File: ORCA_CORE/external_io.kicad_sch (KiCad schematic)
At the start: 24 parts, among them J1 Vext_in, J2 6Vout, J3 6Vout, J4 6Vout, J5 6Vin, J6 Vext_out, J7 6Vout, P1 USB_C_Receptacle_USB2.0, SW1 SW_DPST_x2, U1 FT230XS

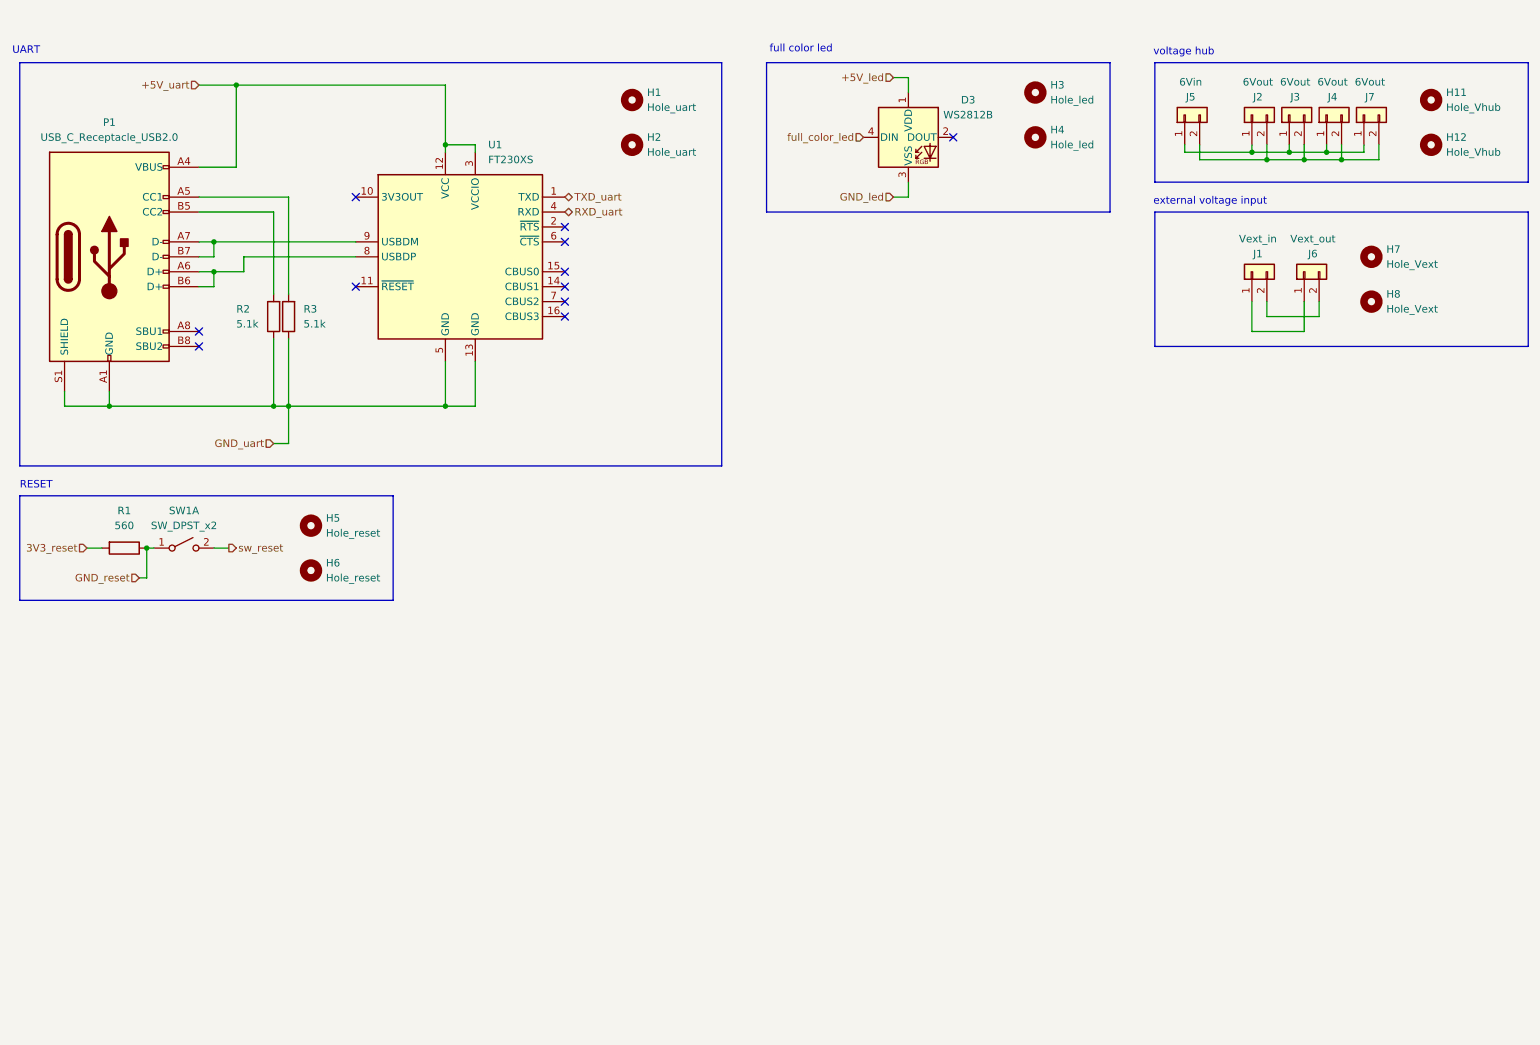
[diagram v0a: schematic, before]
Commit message: complete attaching footprint of CORE
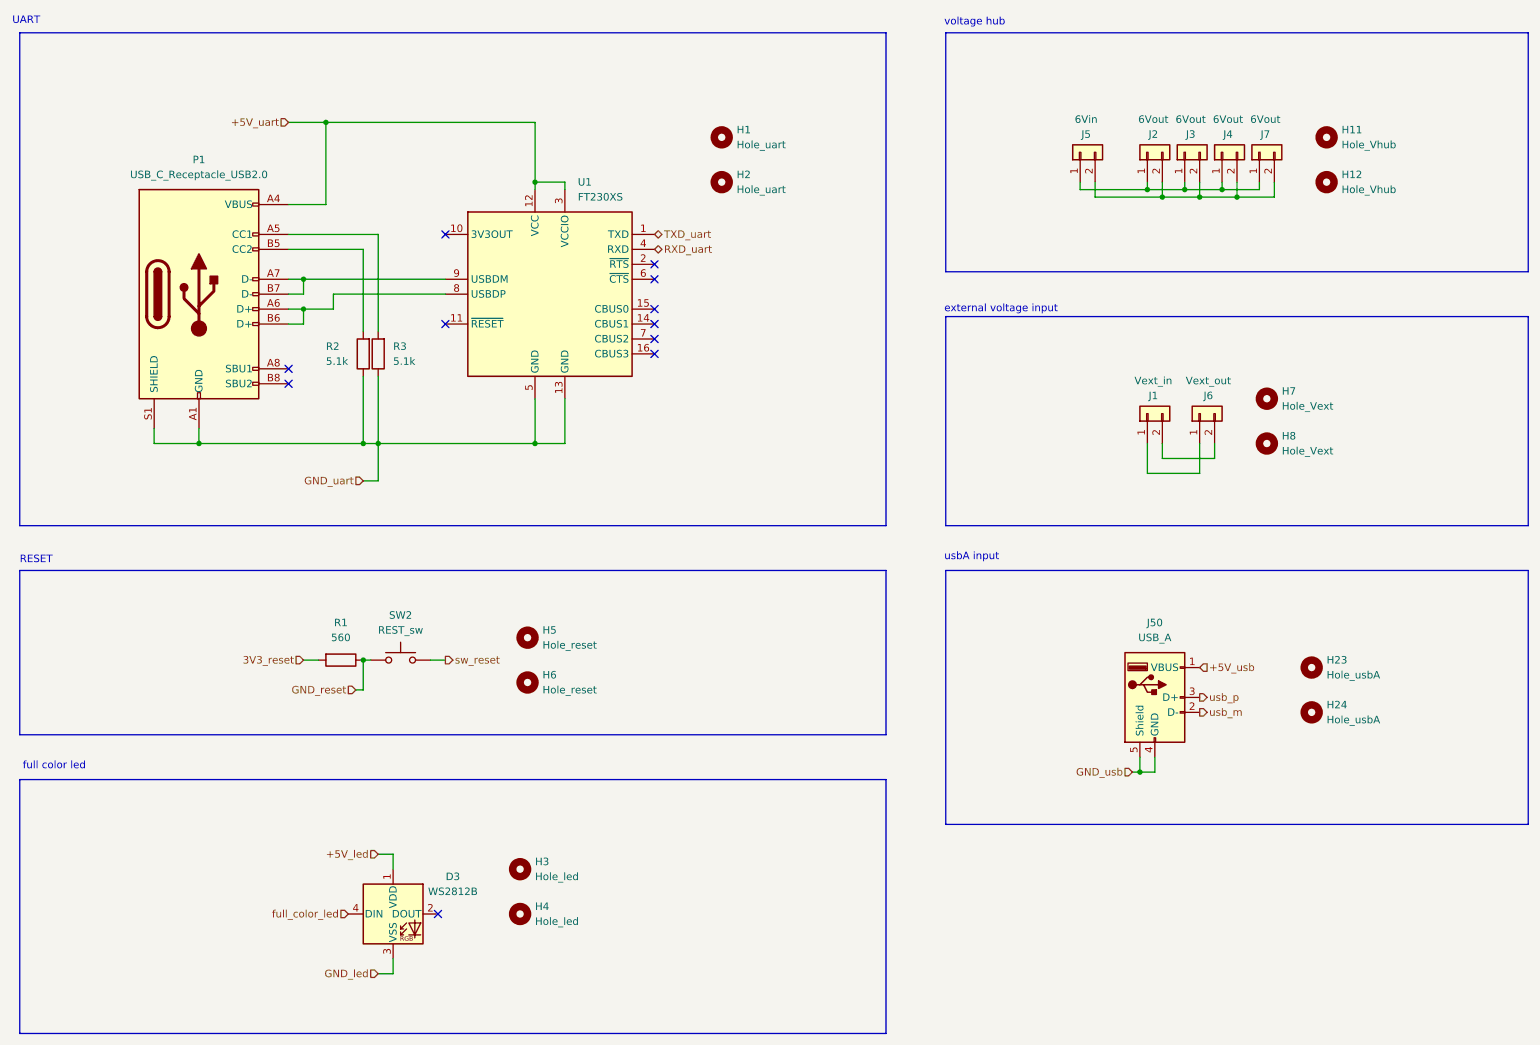
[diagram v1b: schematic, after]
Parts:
- removed SW1: SW_DPST_x2, symbol Switch:SW_DPST_x2
- added H23, H24: Hole_usbA, MountingHole:MountingHole_3.2mm_M3, symbol Mechanical:MountingHole
- added J50: USB_A, Connector_USB:USB_A_Kycon_KUSBX-AS1N-B_Horizontal, symbol Connector:USB_A
- added SW2: REST_sw, Button_Switch_THT:SW_PUSH_6mm, symbol Switch:SW_Push
- R1: footprint (none) -> Resistor_SMD:R_0603_1608Metric_Pad0.98x0.95mm_HandSolder
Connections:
- net GND_reset: now also SW2.1
- net sw_reset: now also SW2.2
- new net +5V_usb: J50.1 (VBUS)
- new net GND_usb: J50.4 (GND), J50.5 (Shield)
- new net usb_m: J50.2 (D-)
- new net usb_p: J50.3 (D+)
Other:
- note added: "usbA input"
- moved on the sheet: D3, H1, H11, H12, H2, H3, H4, H5, H6, H7, H8, J1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

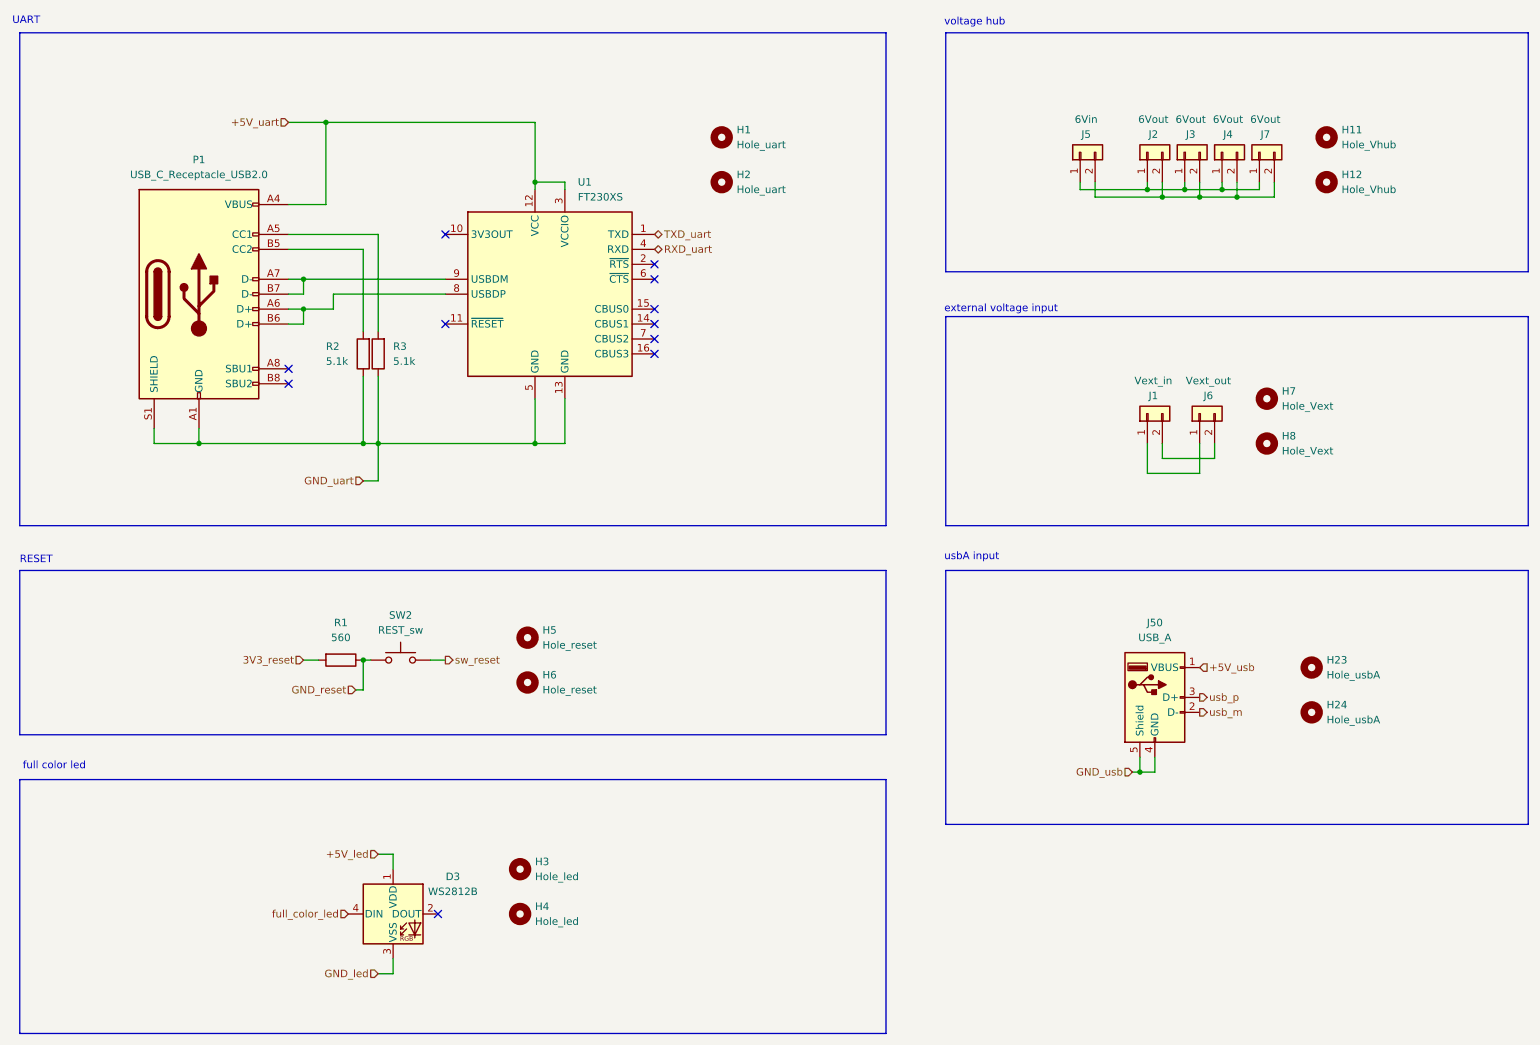
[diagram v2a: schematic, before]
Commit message: connect GND along every boards
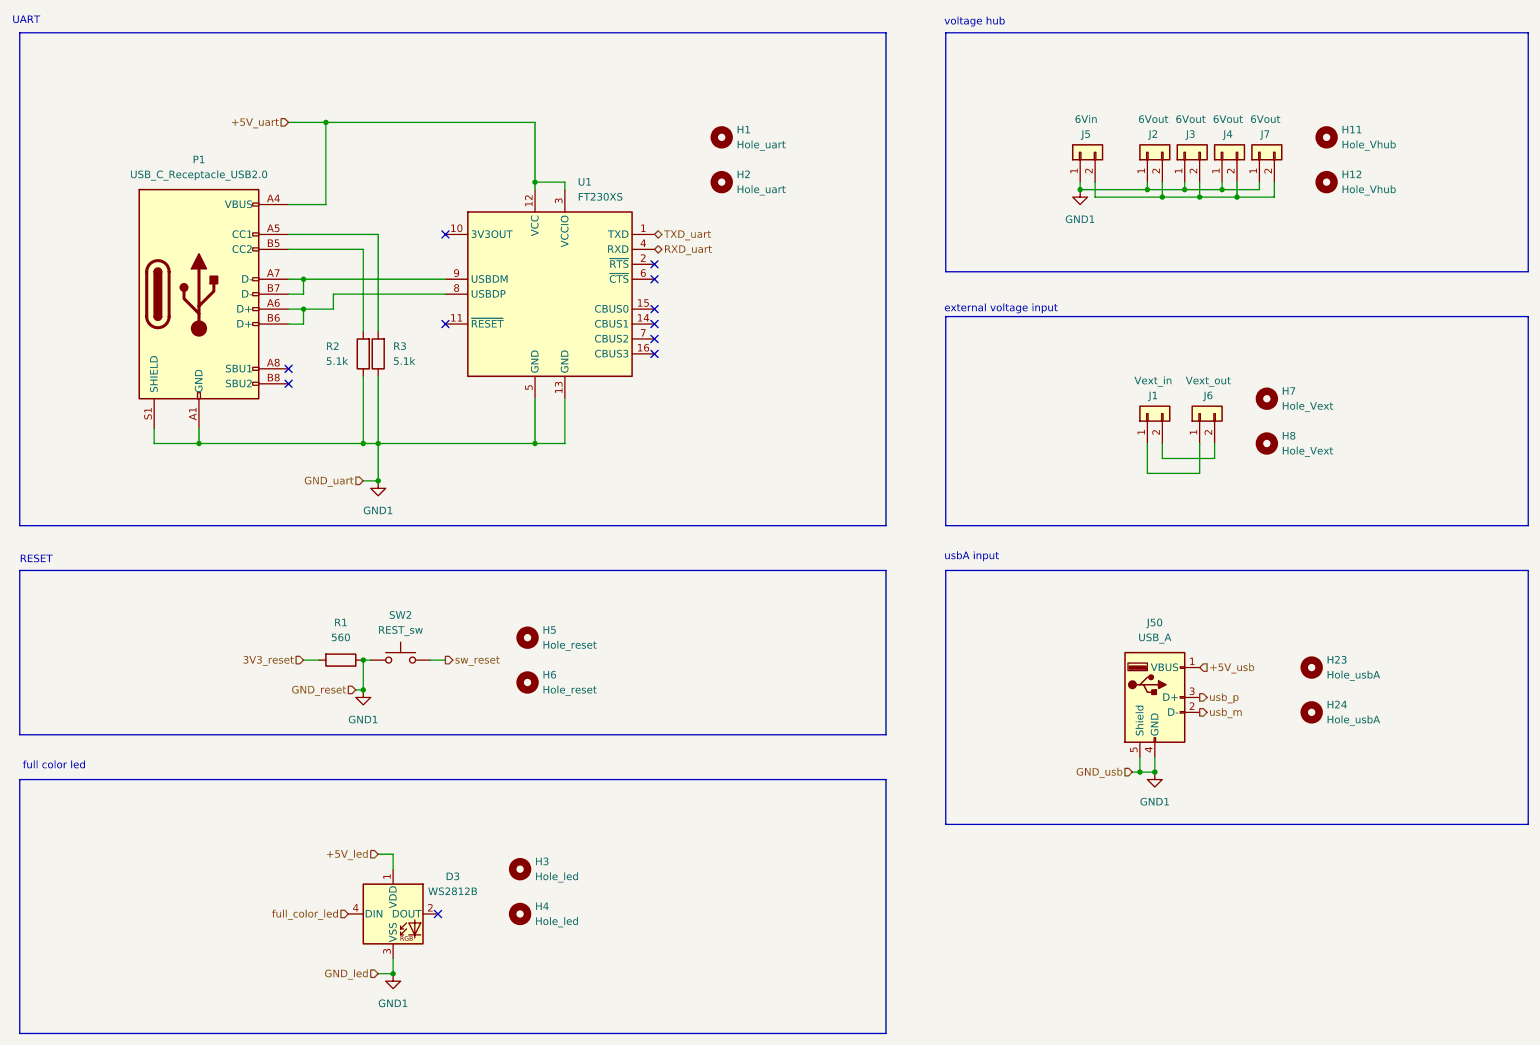
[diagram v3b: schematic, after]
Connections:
- net GND_led is gone; now on net GND1: D3.3 (VSS)
- net GND_reset is gone; now on net GND1: R1.1, SW2.1
- net GND_uart is gone; now on net GND1: P1.A1 (GND), P1.A12 (GND), P1.B1 (GND), P1.B12 (GND), P1.S1 (SHIELD), R2.1, R3.1, U1.13 (GND), U1.5 (GND)
- net GND_usb is gone; now on net GND1: J50.4 (GND), J50.5 (Shield)
- net GND1: now reaches J2.1 (Pin_1), J3.1 (Pin_1), J4.1 (Pin_1), J5.1 (Pin_1), J7.1 (Pin_1)
